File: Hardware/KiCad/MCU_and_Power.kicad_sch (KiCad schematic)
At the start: 34 parts

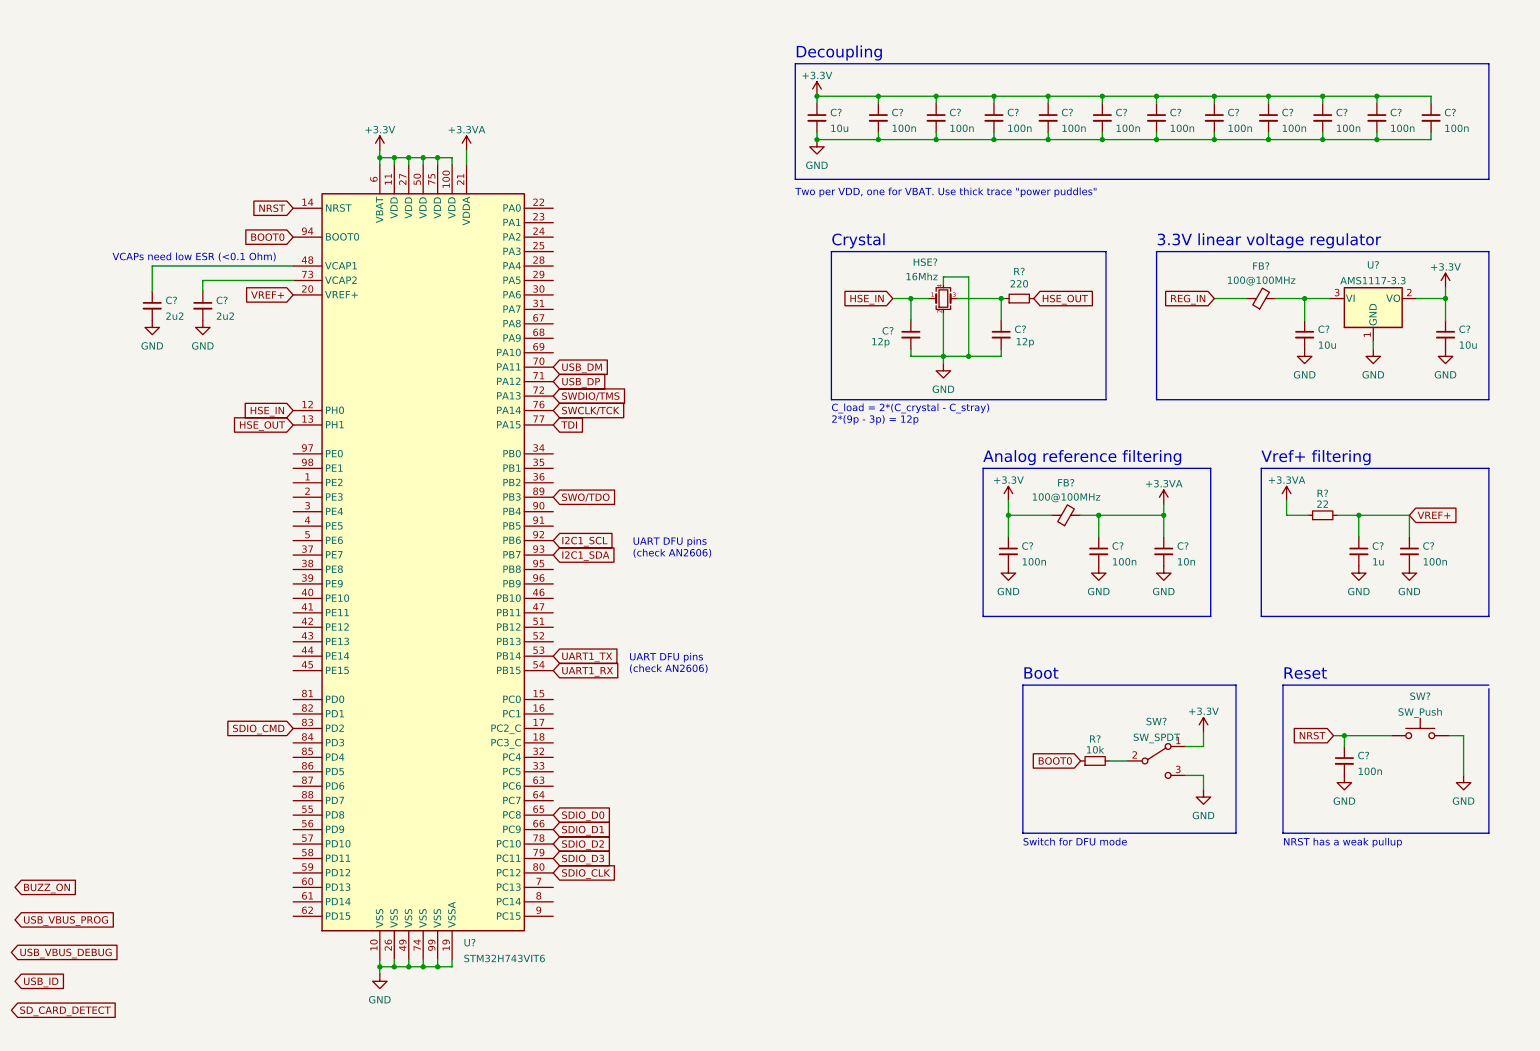
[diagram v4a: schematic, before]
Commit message: Added pinlables, added SD cardholder footprint, fixed VBUS connection, added termination resistors for high frequency signals, improved schematic layout
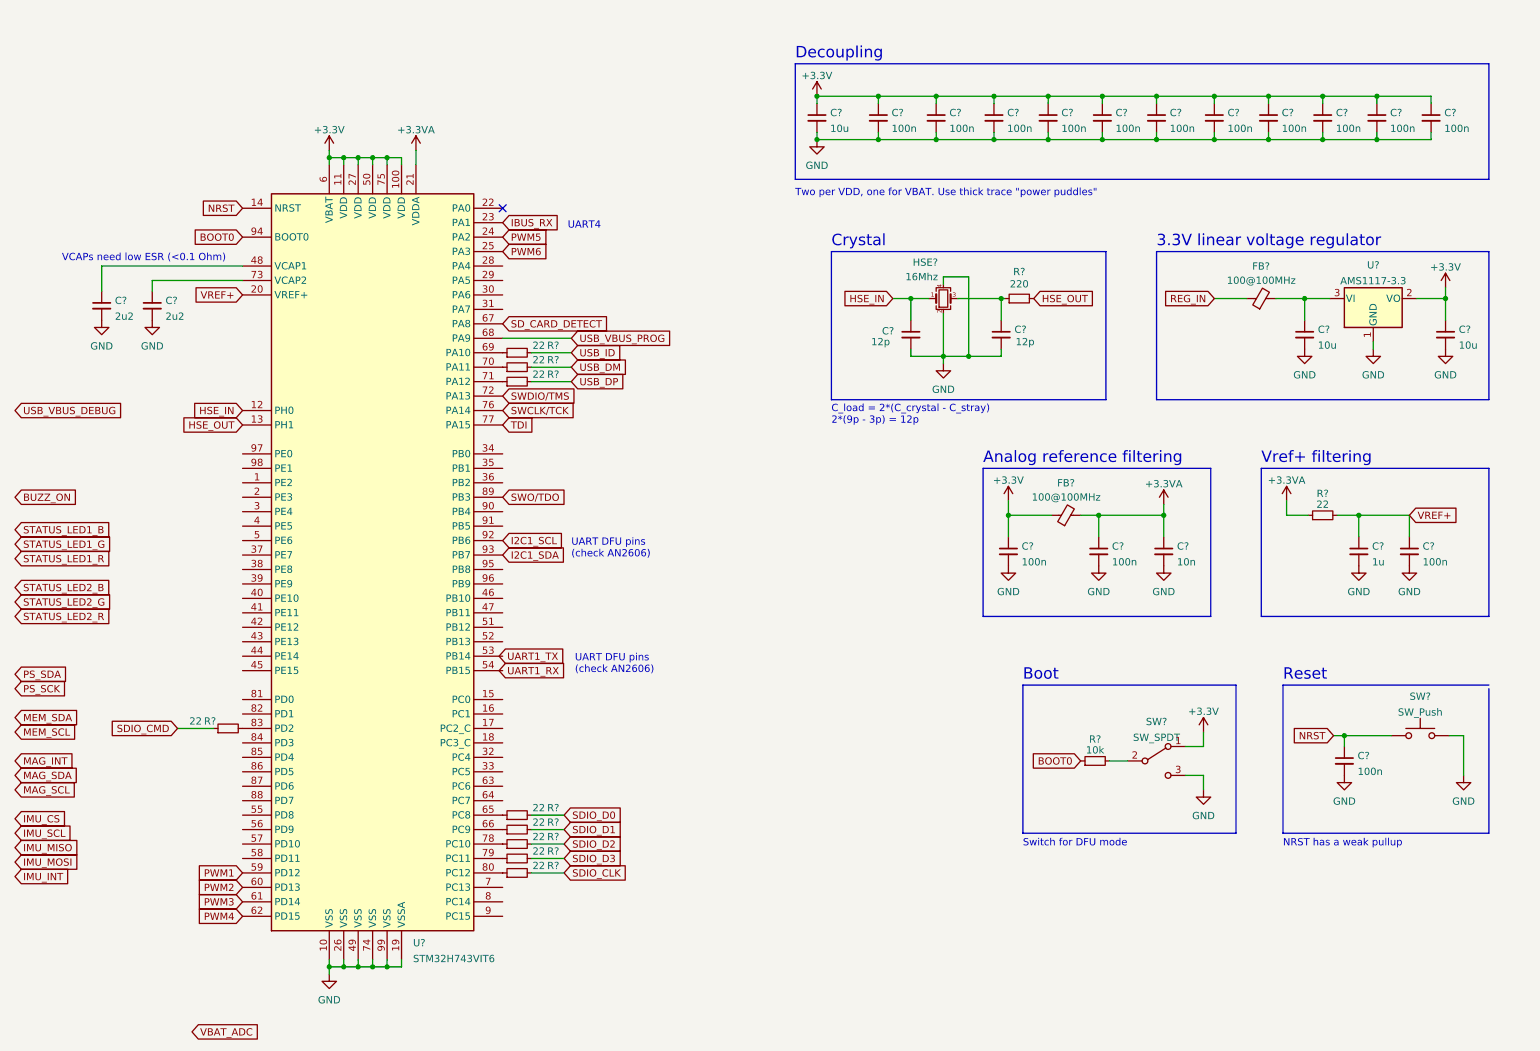
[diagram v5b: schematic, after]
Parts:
- added R? (x9): 22, symbol Device:R_Small
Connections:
- net SDIO_CLK: now also R?.2; no longer U?.80 (PC12)
- net SDIO_CMD: now also R?.1; no longer U?.83 (PD2)
- net SDIO_D0: now also R?.2; no longer U?.65 (PC8)
- net SDIO_D1: now also R?.2; no longer U?.66 (PC9)
- net SDIO_D2: now also R?.2; no longer U?.78 (PC10)
- net SDIO_D3: now also R?.2; no longer U?.79 (PC11)
- net SD_CARD_DETECT: now also U?.67 (PA8)
- net UART1_RX: no longer U?.54 (PB15)
- net UART1_TX: no longer U?.53 (PB14)
- net USB_DM: now also R?.2; no longer U?.70 (PA11)
- net USB_DP: now also R?.2; no longer U?.71 (PA12)
- net USB_ID: now also R?.2
- net USB_VBUS_PROG: now also U?.68 (PA9)
- net IBUS_RX: now reaches U?.23 (PA1)
- net PWM5: now reaches U?.24 (PA2)
- net PWM6: now reaches U?.25 (PA3)
- net PWM1: now reaches U?.59 (PD12)
- net PWM2: now reaches U?.60 (PD13)
- net PWM3: now reaches U?.61 (PD14)
- net PWM4: now reaches U?.62 (PD15)
- net at U?.69 (PA10): now also R?.1
- new net: R?.1, U?.65 (PC8)
- new net: R?.1, U?.66 (PC9)
- new net: R?.1, U?.70 (PA11)
- new net: R?.1, U?.71 (PA12)
- new net: R?.1, U?.78 (PC10)
- new net: R?.1, U?.79 (PC11)
- new net: R?.1, U?.80 (PC12)
- new net: R?.2, U?.83 (PD2)
- no-connect marks 0 -> 1
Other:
- note added: "UART4"
- moved on the sheet: C?, U?

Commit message: More pin definitions
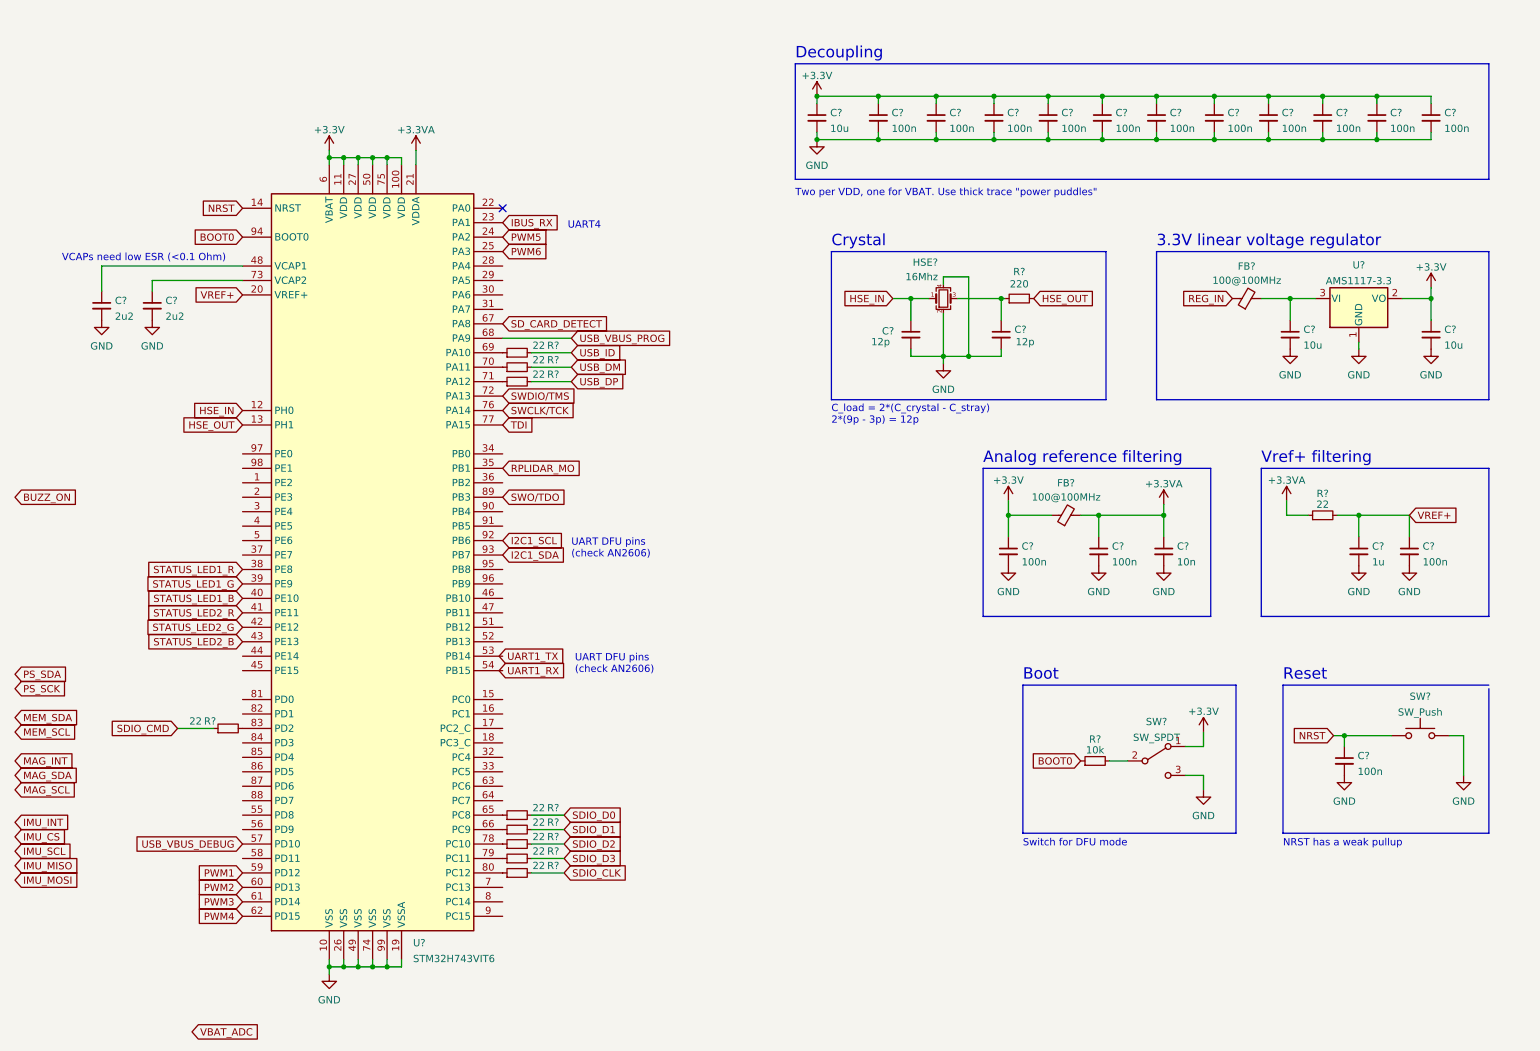
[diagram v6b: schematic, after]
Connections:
- net STATUS_LED1_B: now also U?.40 (PE10)
- net STATUS_LED1_G: now also U?.39 (PE9)
- net STATUS_LED1_R: now also U?.38 (PE8)
- net STATUS_LED2_B: now also U?.43 (PE13)
- net STATUS_LED2_G: now also U?.42 (PE12)
- net STATUS_LED2_R: now also U?.41 (PE11)
- net USB_VBUS_DEBUG: now also U?.57 (PD10)
- net RPLIDAR_MO: now reaches U?.35 (PB1)
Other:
- moved on the sheet: C?, FB?, U?

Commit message: Added pullups, testpoints and more pin definitions
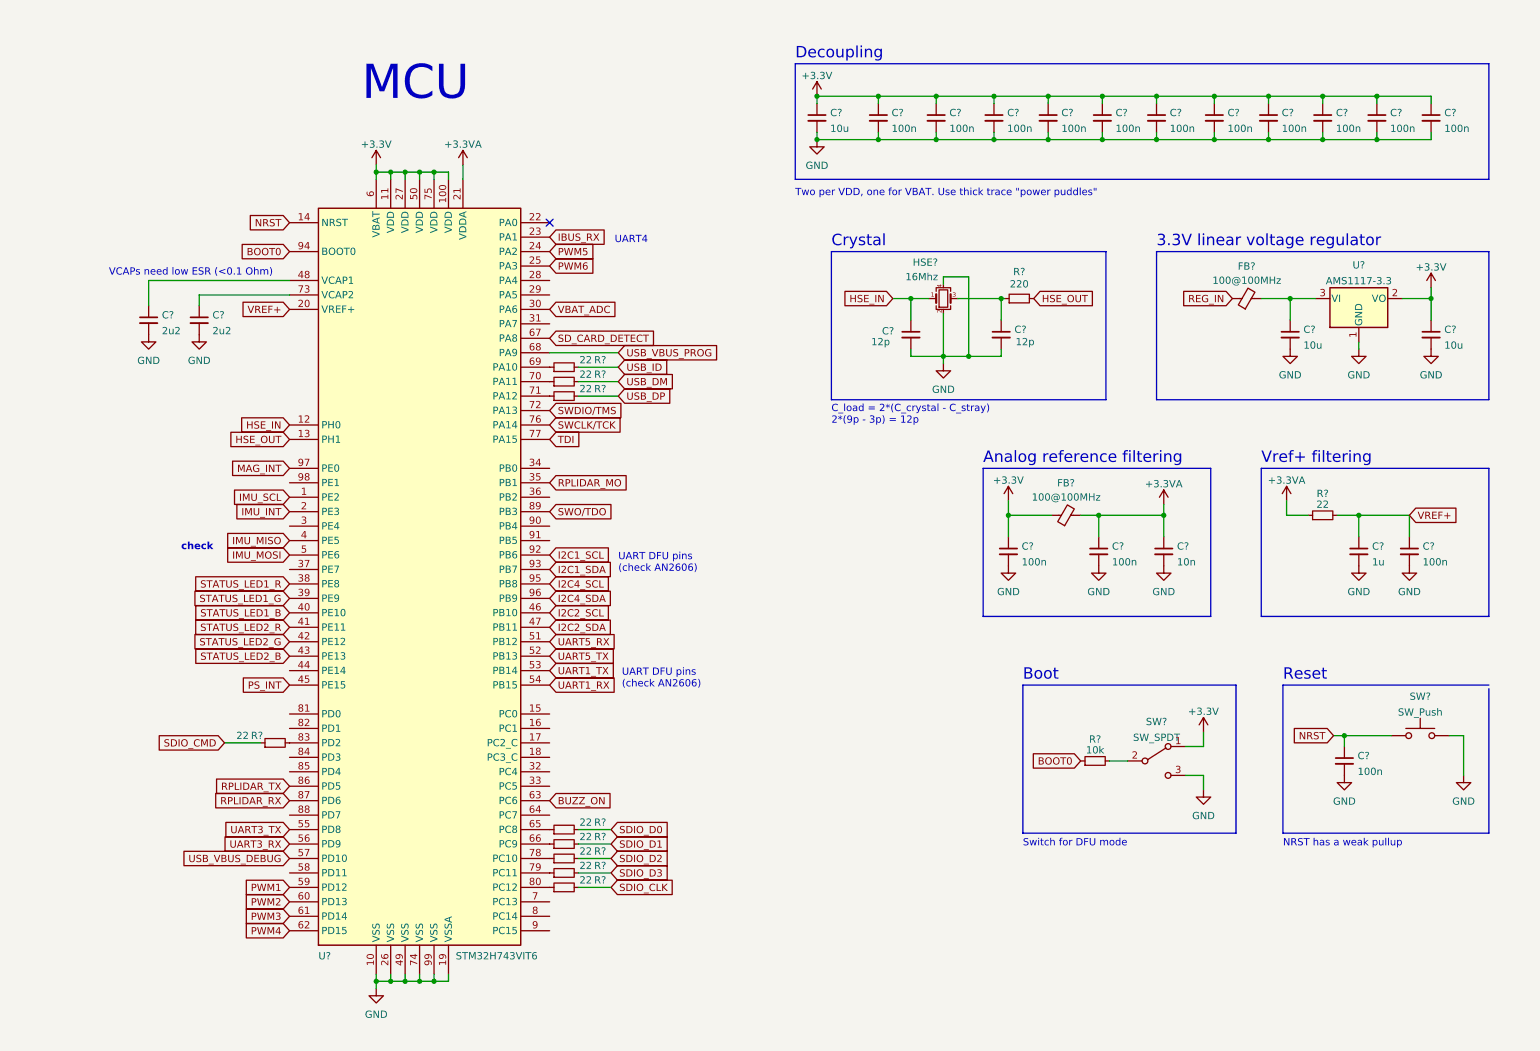
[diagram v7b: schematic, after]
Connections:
- net BUZZ_ON: now also U?.63 (PC6)
- net IMU_INT: now also U?.2 (PE3)
- net IMU_MISO: now also U?.4 (PE5)
- net IMU_MOSI: now also U?.5 (PE6)
- net IMU_SCL: now also U?.1 (PE2)
- net MAG_INT: now also U?.97 (PE0)
- net UART1_RX: now also U?.54 (PB15)
- net UART1_TX: now also U?.53 (PB14)
- net VBAT_ADC: now also U?.30 (PA6)
- net PS_INT: now reaches U?.45 (PE15)
- net I2C2_SCL: now reaches U?.46 (PB10)
- net I2C2_SDA: now reaches U?.47 (PB11)
- net UART5_RX: now reaches U?.51 (PB12)
- net UART5_TX: now reaches U?.52 (PB13)
- net UART3_TX: now reaches U?.55 (PD8)
- net UART3_RX: now reaches U?.56 (PD9)
- net RPLIDAR_TX: now reaches U?.86 (PD5)
- net RPLIDAR_RX: now reaches U?.87 (PD6)
- net I2C4_SCL: now reaches U?.95 (PB8)
- net I2C4_SDA: now reaches U?.96 (PB9)
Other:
- note added: "MCU"
- note added: "check"
- moved on the sheet: C?, R?, U?
